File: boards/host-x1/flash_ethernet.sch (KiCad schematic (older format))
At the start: 81 parts, among them J4 BEL_FUSE_0826-1G1T-23-F, Q1 SSM6N58NU, Q2 SSM6N58NU, Q3 SSM6N58NU, Q4 SSM6N58NU, U10 DSC6102CI2A-100.0000, U11 S25FS064S_BGA, U2 XC7A100T-1FTG256C, U8 KSZ9031RN, U9 DSC6101CI2A-025.0000

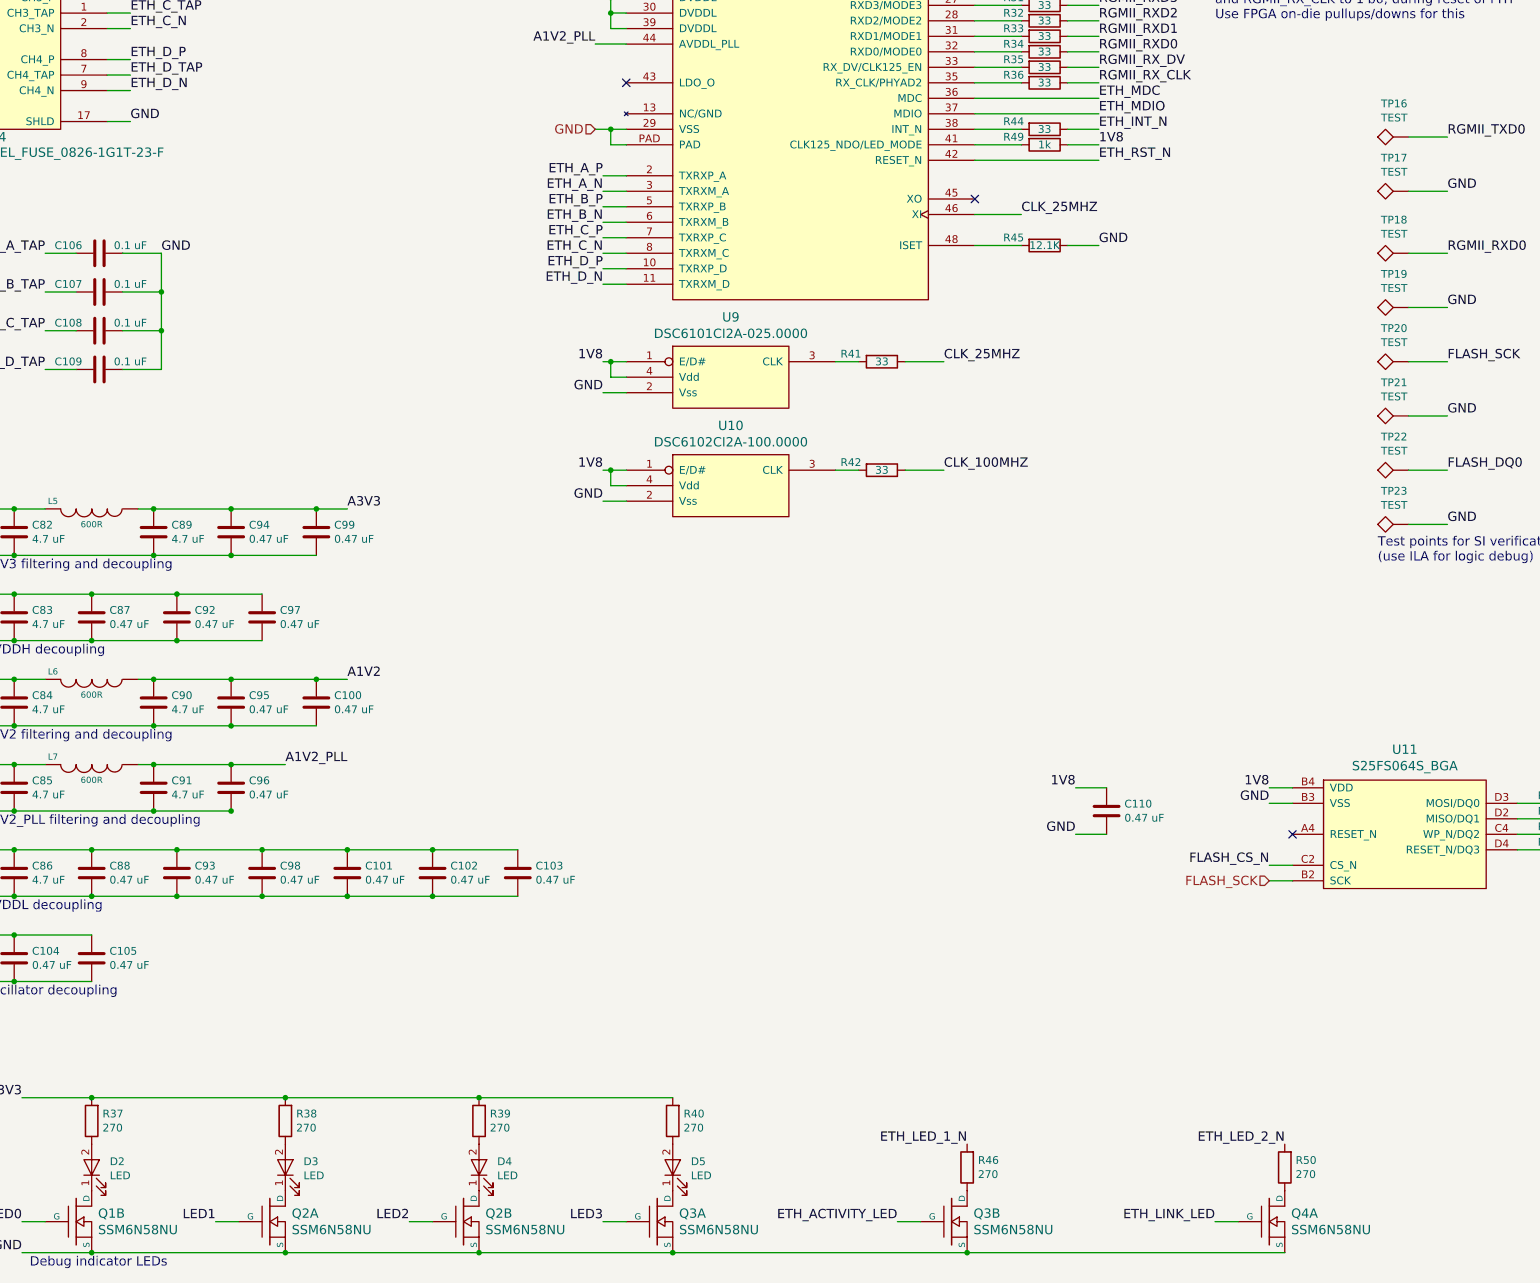
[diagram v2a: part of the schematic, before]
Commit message: Finished initial schematic and component assignments, ready for layout
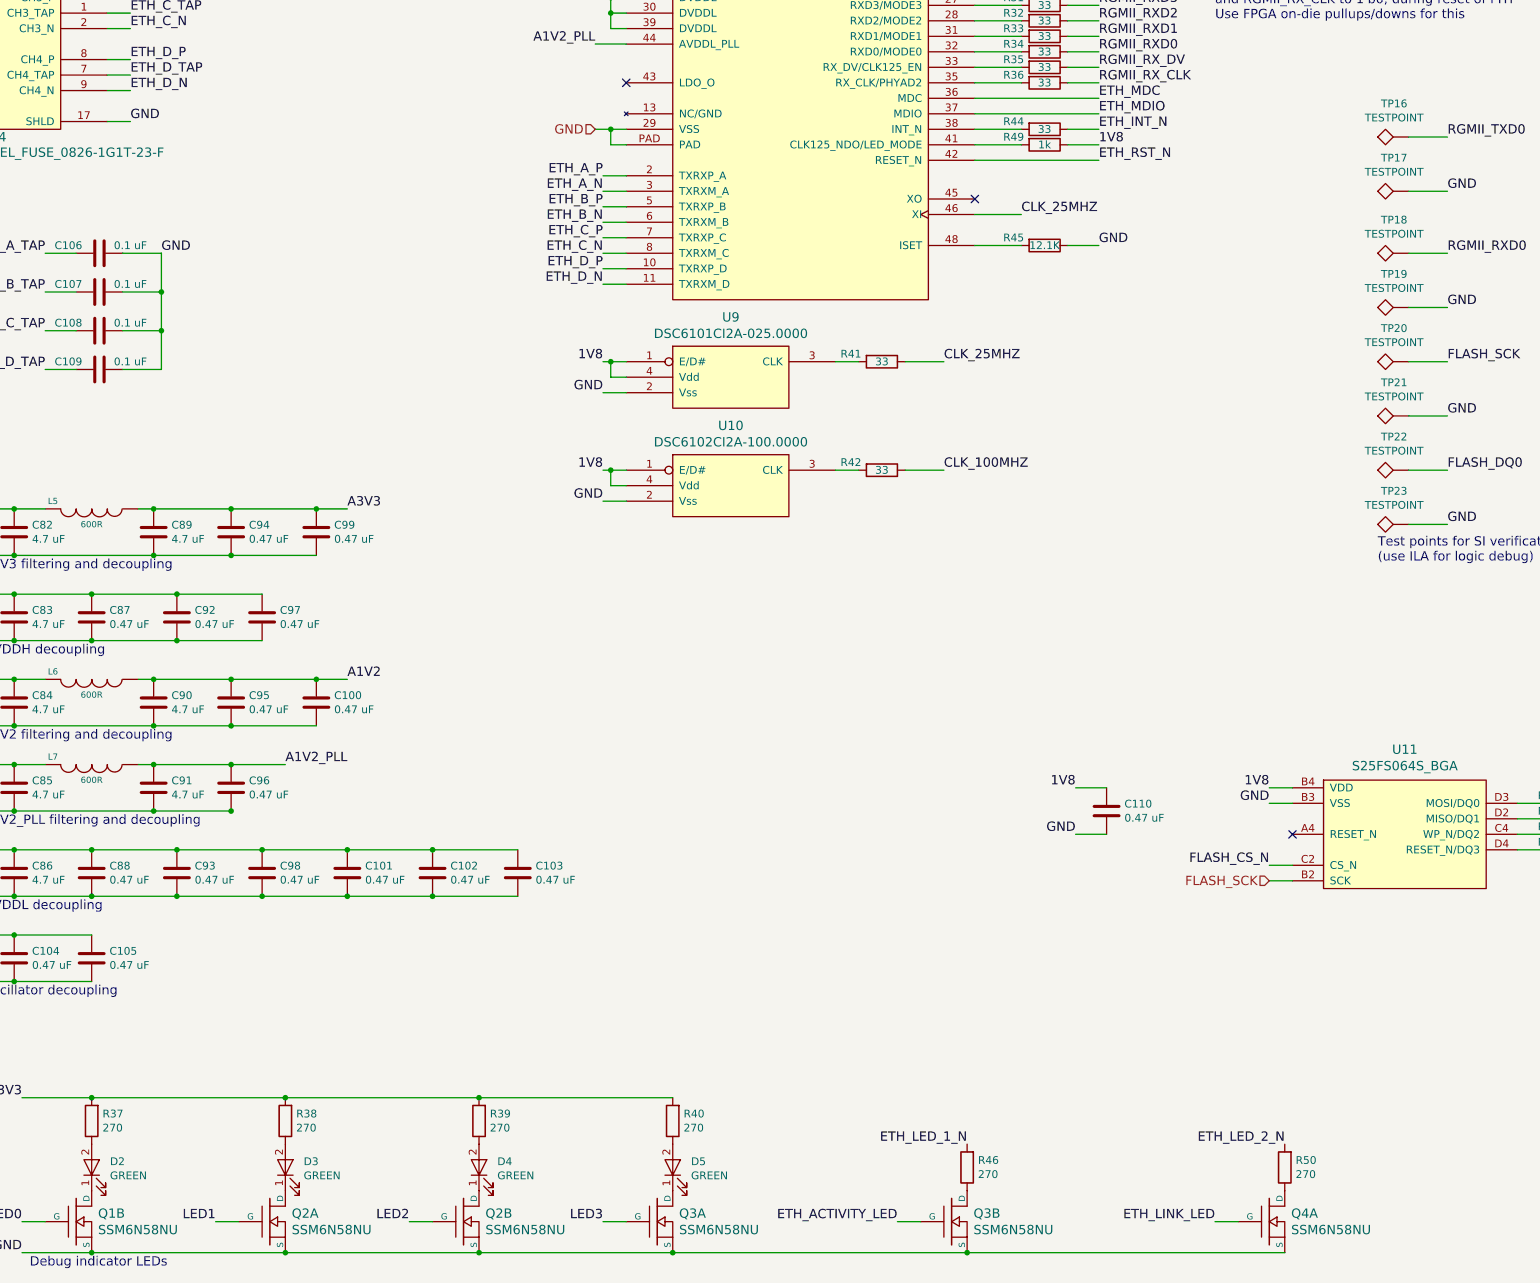
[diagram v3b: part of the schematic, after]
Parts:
- C100, C101, C102, C103, C104, C105, C106, C107, C108, C109, C110, C87, C88, C92, C93, C94, C95, C96, C97, C98, C99: footprint (none) -> azonenberg_pcb:EIA_0402_CAP_NOSILK
- C82, C83, C84, C85, C86, C89, C90, C91: footprint (none) -> azonenberg_pcb:EIA_0603_CAP_NOSILK
- D2, D3, D4, D5: value LED -> GREEN; footprint (none) -> azonenberg_pcb:EIA_0603_LED
- J4: footprint (none) -> azonenberg_pcb:CONN_BELFUSE_0826_1G1T_23_F
- L5, L6, L7, R28, R29, R30, R31, R32, R33, R34, R35, R36, R37, R38, R39, R40, R41, R42, R43, R44, R45, R46, R47, R48, R49, R50, R51, R52, R53, R54: footprint (none) -> azonenberg_pcb:EIA_0402_RES_NOSILK
- Q1, Q2, Q3, Q4: footprint (none) -> azonenberg_pcb:DFN_6_0.65MM_2x2MM_GDS
- TP16, TP17, TP18, TP19, TP20, TP21, TP22, TP23: value TEST -> TESTPOINT; footprint (none) -> azonenberg_pcb:TESTPOINT_BARETRACE_150UM
- U10, U9: footprint (none) -> azonenberg_pcb:OSCILLATOR_3.2x2.5
- U11: footprint (none) -> azonenberg_pcb:BGA_24_6x8_DEPOP1_1MM
- U2: footprint (none) -> azonenberg_pcb:BGA_256_17x17_FULLARRAY_1MM
- U8: footprint (none) -> azonenberg_pcb:QFN_48_0.5MM_7x7MM

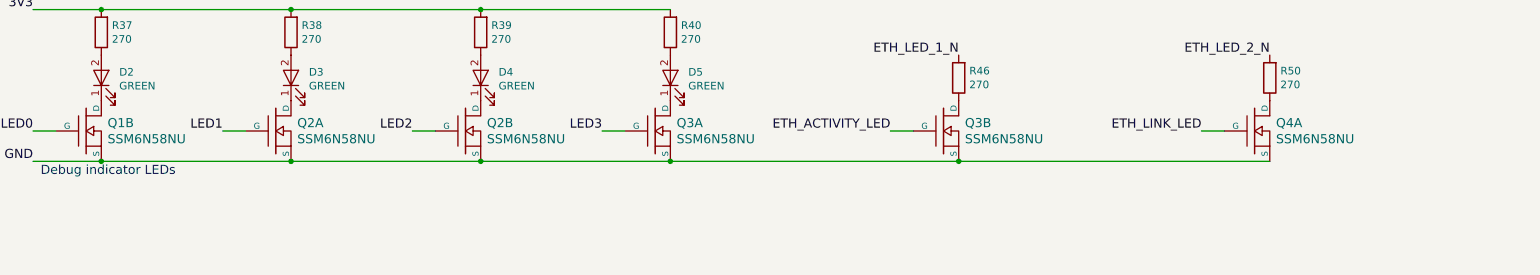
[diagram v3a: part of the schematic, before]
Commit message: Finished initial component group placement
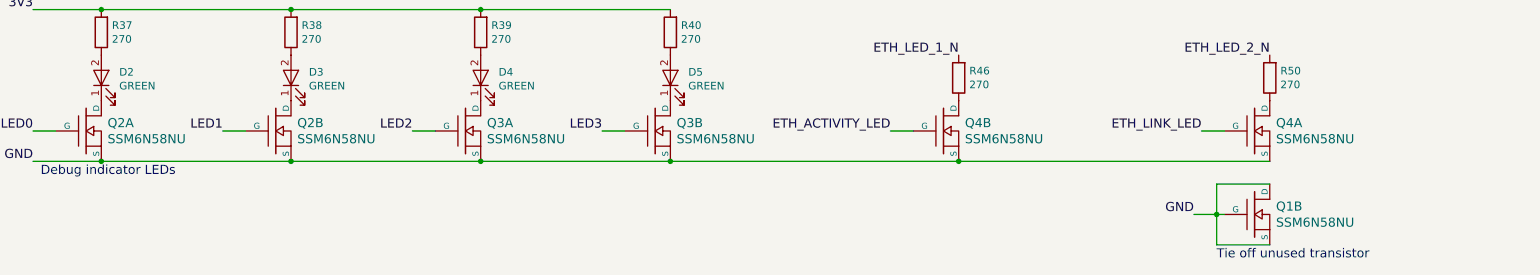
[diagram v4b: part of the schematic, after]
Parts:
- added unit 2 of Q4
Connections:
- net ETH_ACTIVITY_LED: now also Q4.G2 (G); no longer Q3.G2 (G)
- net GND: now also Q1.D2 (D), Q1.G2 (G), Q4.S2 (S)
- net LED0: now also Q2.G1 (G); no longer Q1.G2 (G)
- net LED1: now also Q2.G2 (G); no longer Q2.G1 (G)
- net LED2: now also Q3.G1 (G); no longer Q2.G2 (G)
- net LED3: now also Q3.G2 (G); no longer Q3.G1 (G)
- net at D2.1 (K): now also Q2.D1 (D); no longer Q1.D2 (D)
- net at D3.1 (K): now also Q2.D2 (D); no longer Q2.D1 (D)
- net at D4.1 (K): now also Q3.D1 (D); no longer Q2.D2 (D)
- net at D5.1 (K): now also Q3.D2 (D); no longer Q3.D1 (D)
- net at R46.1: now also Q4.D2 (D); no longer Q3.D2 (D)
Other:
- note added: "Tie off unused transistor"
- moved on the sheet: Q1B, Q2A, Q2B, Q3A, Q3B
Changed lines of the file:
@@
 EESchema Schematic File Version 2
+LIBS:host-x1-rescue
 LIBS:conn
 LIBS:device
@@
 L SSM6N58NU_DUAL_NMOS Q1
 U 2 1 5910F2D1
-P 1500 10100
-F 0 "Q1" H 1641 10153 60  0000 L CNN
-F 1 "SSM6N58NU" H 1641 10047 60  0000 L CNN
-F 2 "azonenberg_pcb:DFN_6_0.65MM_2x2MM_GDS" H 1500 10100 60  0001 C CNN
-F 3 "" H 1500 10100 60  0000 C CNN
-	2    1500 10100
+P 9200 10650
+F 0 "Q1" H 9341 10703 60  0000 L CNN
+F 1 "SSM6N58NU" H 9341 10597 60  0000 L CNN
+F 2 "azonenberg_pcb:DFN_6_0.65MM_2x2MM_GDS" H 9200 10650 60  0001 C CNN
+F 3 "" H 9200 10650 60  0000 C CNN
+	2    9200 10650
 	1    0    0    -1
 $EndComp
@@
 L SSM6N58NU_DUAL_NMOS Q2
 U 1 1 59110611
-P 2750 10100
-F 0 "Q2" H 2891 10153 60  0000 L CNN
-F 1 "SSM6N58NU" H 2891 10047 60  0000 L CNN
-F 2 "azonenberg_pcb:DFN_6_0.65MM_2x2MM_GDS" H 2750 10100 60  0001 C CNN
-F 3 "" H 2750 10100 60  0000 C CNN
-	1    2750 10100
+P 1500 10100
+F 0 "Q2" H 1641 10153 60  0000 L CNN
+F 1 "SSM6N58NU" H 1641 10047 60  0000 L CNN
+F 2 "azonenberg_pcb:DFN_6_0.65MM_2x2MM_GDS" H 1500 10100 60  0001 C CNN
+F 3 "" H 1500 10100 60  0000 C CNN
+	1    1500 10100
 	1    0    0    -1
 $EndComp
@@
 L SSM6N58NU_DUAL_NMOS Q2
 U 2 1 591108D0
-P 4000 10100
-F 0 "Q2" H 4141 10153 60  0000 L CNN
-F 1 "SSM6N58NU" H 4141 10047 60  0000 L CNN
-F 2 "azonenberg_pcb:DFN_6_0.65MM_2x2MM_GDS" H 4000 10100 60  0001 C CNN
-F 3 "" H 4000 10100 60  0000 C CNN
-	2    4000 10100
+P 2750 10100
+F 0 "Q2" H 2891 10153 60  0000 L CNN
+F 1 "SSM6N58NU" H 2891 10047 60  0000 L CNN
+F 2 "azonenberg_pcb:DFN_6_0.65MM_2x2MM_GDS" H 2750 10100 60  0001 C CNN
+F 3 "" H 2750 10100 60  0000 C CNN
+	2    2750 10100
 	1    0    0    -1
 $EndComp
@@
 L SSM6N58NU_DUAL_NMOS Q3
 U 1 1 59110B5B
-P 5250 10100
-F 0 "Q3" H 5391 10153 60  0000 L CNN
-F 1 "SSM6N58NU" H 5391 10047 60  0000 L CNN
-F 2 "azonenberg_pcb:DFN_6_0.65MM_2x2MM_GDS" H 5250 10100 60  0001 C CNN
-F 3 "" H 5250 10100 60  0000 C CNN
-	1    5250 10100
+P 4000 10100
+F 0 "Q3" H 4141 10153 60  0000 L CNN
+F 1 "SSM6N58NU" H 4141 10047 60  0000 L CNN
+F 2 "azonenberg_pcb:DFN_6_0.65MM_2x2MM_GDS" H 4000 10100 60  0001 C CNN
+F 3 "" H 4000 10100 60  0000 C CNN
+	1    4000 10100
 	1    0    0    -1
 $EndComp
@@
 L SSM6N58NU_DUAL_NMOS Q3
 U 2 1 59122A75
-P 7150 10100
-F 0 "Q3" H 7291 10153 60  0000 L CNN
-F 1 "SSM6N58NU" H 7291 10047 60  0000 L CNN
-F 2 "azonenberg_pcb:DFN_6_0.65MM_2x2MM_GDS" H 7150 10100 60  0001 C CNN
-F 3 "" H 7150 10100 60  0000 C CNN
-	2    7150 10100
+P 5250 10100
+F 0 "Q3" H 5391 10153 60  0000 L CNN
+F 1 "SSM6N58NU" H 5391 10047 60  0000 L CNN
+F 2 "azonenberg_pcb:DFN_6_0.65MM_2x2MM_GDS" H 5250 10100 60  0001 C CNN
+F 3 "" H 5250 10100 60  0000 C CNN
+	2    5250 10100
 	1    0    0    -1
 $EndComp
@@
 Text Notes 9900 5850 0    60   ~ 0
 Test points for SI verification\n(use ILA for logic debug)
+$Comp
+L SSM6N58NU_DUAL_NMOS Q4
+U 2 1 5910409D
+P 7150 10100
+F 0 "Q4" H 7291 10153 60  0000 L CNN
+F 1 "SSM6N58NU" H 7291 10047 60  0000 L CNN
+F 2 "azonenberg_pcb:DFN_6_0.65MM_2x2MM_GDS" H 7150 10100 60  0001 C CNN
+F 3 "" H 7150 10100 60  0000 C CNN
+	2    7150 10100
+	1    0    0    -1
+$EndComp
+Text Label 8800 10650 2    60   ~ 0
+GND
+Wire Wire Line
+	8800 10650 9000 10650
+Wire Wire Line
+	8950 10450 9300 10450
+Wire Wire Line
+	8950 10450 8950 10850
+Connection ~ 8950 10650
+Wire Wire Line
+	8950 10850 9300 10850
+Text Notes 8950 10950 0    60   ~ 0
+Tie off unused transistor
 $EndSCHEMATC
